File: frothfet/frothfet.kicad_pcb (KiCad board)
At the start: 4 copper layers, 144 x 127 mm, 251 parts, among them J1 Conn_01x01, J10 Screw_Terminal_01x08, J11 Screw_Terminal_01x08, J2 Conn_01x01, J3 Conn_01x01, J4 Conn_01x01, J5 Conn_01x01, J6 Conn_01x01, J7 Conn_01x01, J8 Conn_01x01, J9 Conn_01x03_Pin, Q1 BSC010N04LS, Q10 2N7002, Q2 BSC010N04LS, Q3 BSC010N04LS, Q4 BSC010N04LS, Q5 BSC010N04LS, Q6 BSC010N04LS, Q7 BSC010N04LS, Q8 BSC010N04LS, Q9 2N7002, U10 LTC7004EMSE-PBF, U11 ACS725xLCTR-20AU, U12 LTC7004EMSE-PBF, U13 ACS725xLCTR-20AU, U14 LTC7004EMSE-PBF, U15 ACS725xLCTR-20AU, U16 LTC7004EMSE-PBF, U17 ACS725xLCTR-20AU, U18 MCP3564R, U19 MCP1502-33, U2 LTC7004EMSE-PBF, U20 MCP3425A0T-ECH, U21 XL1509-5.0, U22 ADS1015IDGS, U23 ADS1015IDGS, U24 MCP1754S-3302xCB, U3 ACS725xLCTR-20AU, U4 LTC7004EMSE-PBF, U5 ACS725xLCTR-20AU, U6 LTC7004EMSE-PBF, U7 ACS725xLCTR-20AU, U8 LTC7004EMSE-PBF, U9 ACS725xLCTR-20AU

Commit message: drc passing
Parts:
- U1: value ~ -> ESP32-S3-DEVKITC
- moved REF** 35.1 mm to (56.0, 83.0)
- moved LOGO1 18.6 mm to (66.8, 83.0)
- moved U21 0.75 mm to (74.2, 42.5)
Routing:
- net GND: track 443.3 -> 260.3 mm, vias 108 -> 145
- net +5V: track 454.3 -> 335.1 mm, vias 17 -> 10
- net Net-(Q6-G): track 62.5 -> 31.2 mm
- net Net-(Q8-G): track 62.5 -> 31.2 mm
- net Net-(Q7-G): track 62.5 -> 31.2 mm
- net Net-(Q4-G): track 62.5 -> 31.2 mm
- net Net-(Q5-G): track 62.5 -> 31.2 mm
- net Net-(Q3-G): track 62.5 -> 31.2 mm
- net Net-(Q2-G): track 62.5 -> 31.2 mm
- net +3.3V: track 547.9 -> 576.4 mm, vias 16 -> 10
- net Net-(U10-TGUP): track 54.0 -> 27.0 mm
- net Net-(U8-TGUP): track 54.0 -> 27.0 mm
- net Net-(U14-TGUP): track 54.0 -> 27.0 mm
- net Net-(U16-TGUP): track 54.0 -> 27.0 mm
- net Net-(U12-TGUP): track 54.0 -> 27.0 mm
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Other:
- board text added: "3V3"
- board text added: "FrothFET 8CH"
- board text added: "MPC"
- board text added: "VREF SEL"
- board text removed: "FrothFET 12CH"

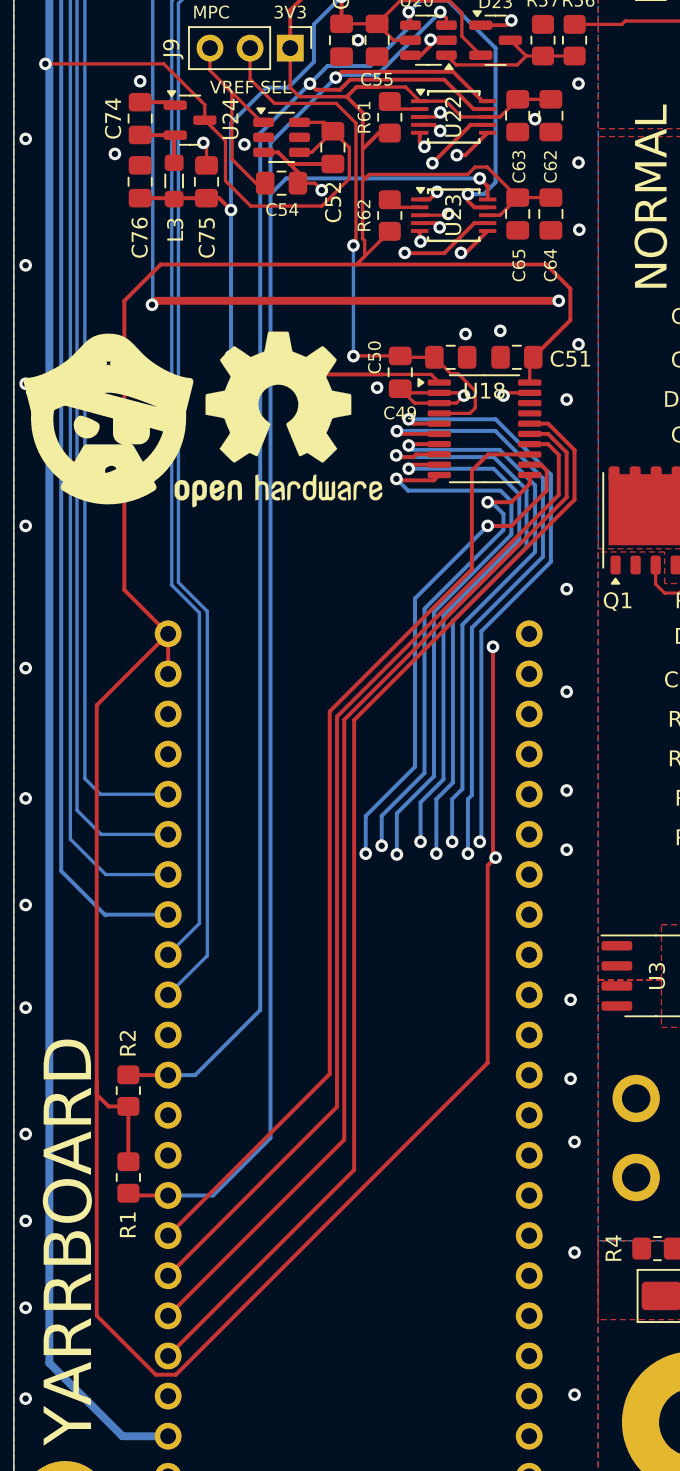
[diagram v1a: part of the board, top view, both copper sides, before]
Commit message: fatter power trace and layer 3 is fully ground plane now.
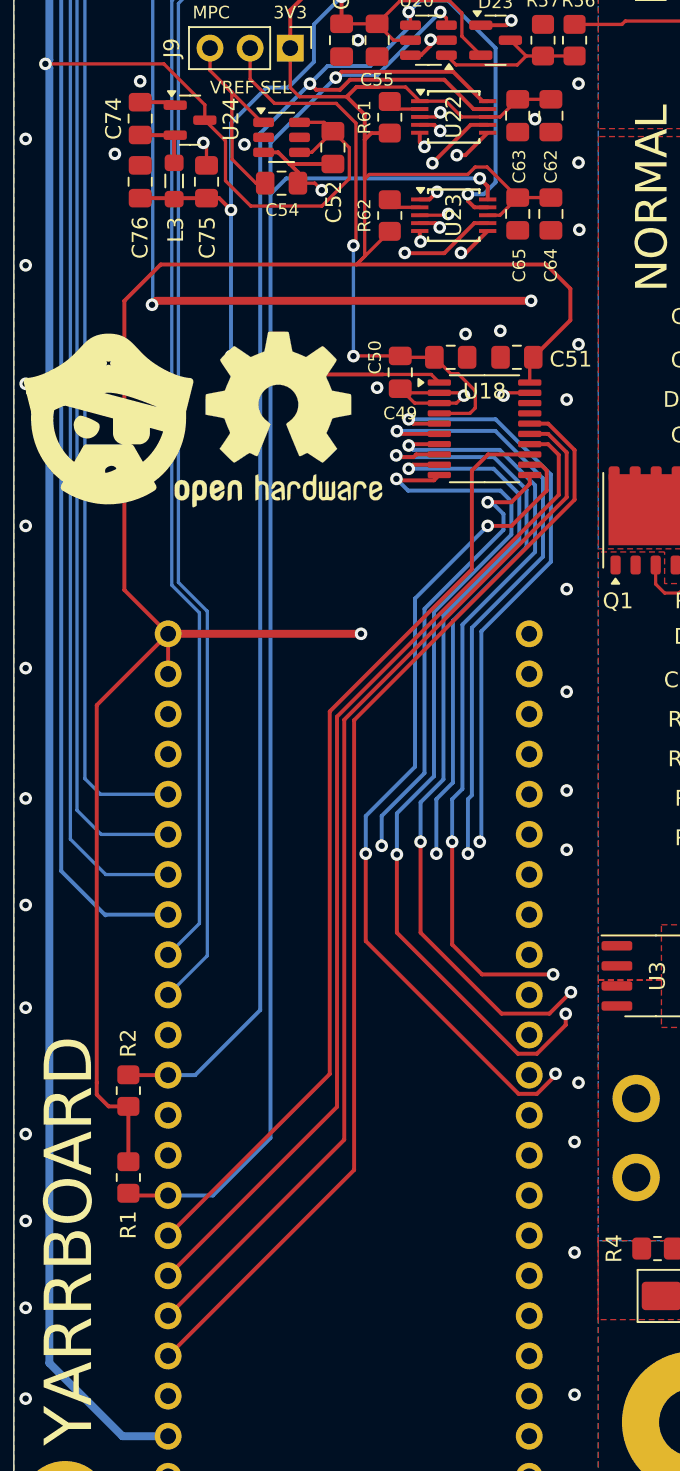
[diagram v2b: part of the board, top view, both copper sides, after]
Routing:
- net +3.3V: track 576.4 -> 518.5 mm, vias 10 -> 9
- net /CHANNEL 8/CURRENT_ADC: track 171.8 -> 163.7 mm, vias 3 -> 4
- net /CHANNEL 4/PWM: track 85.6 -> 78.5 mm
- net /CHANNEL 7/CURRENT_ADC: track 152.9 -> 145.9 mm
- net /CHANNEL 6/PWM: track 108.4 -> 101.9 mm
- net /CHANNEL 3/PWM: track 64.2 -> 60.0 mm
- net /CHANNEL 2/PWM: track 49.5 -> 46.1 mm
- net /CHANNEL 5/CURRENT_ADC: track 125.4 -> 122.1 mm, vias 3 -> 4
- net /CHANNEL 6/CURRENT_ADC: track 142.7 -> 139.6 mm, vias 3 -> 4
- net /CHANNEL 2/CURRENT_ADC: track 80.0 -> 83.0 mm
- net /CHANNEL 5/PWM: track 94.7 -> 91.9 mm
- net /CHANNEL 3/CURRENT_ADC: track 93.6 -> 94.9 mm, vias 3 -> 4
- net /CHANNEL 1/CURRENT_ADC: track 64.7 -> 65.9 mm
- net GND: vias 145 -> 144

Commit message: reannotate
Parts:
- C14, C2, C20, C26, C32, C38, C44, C8: value 100nF/50v -> 100nF
- C66, C67, C68, C69, C70, C71, C72, C73: value .47uF/50v -> 470nF/50v
